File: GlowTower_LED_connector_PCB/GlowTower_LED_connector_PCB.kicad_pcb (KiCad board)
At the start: 2 copper layers, 38 x 38 mm, 12 parts, among them SW1 TS-1102S-C-A-B, U1 LED strip, U2 LED strip, U3 LED strip, U4 LED strip

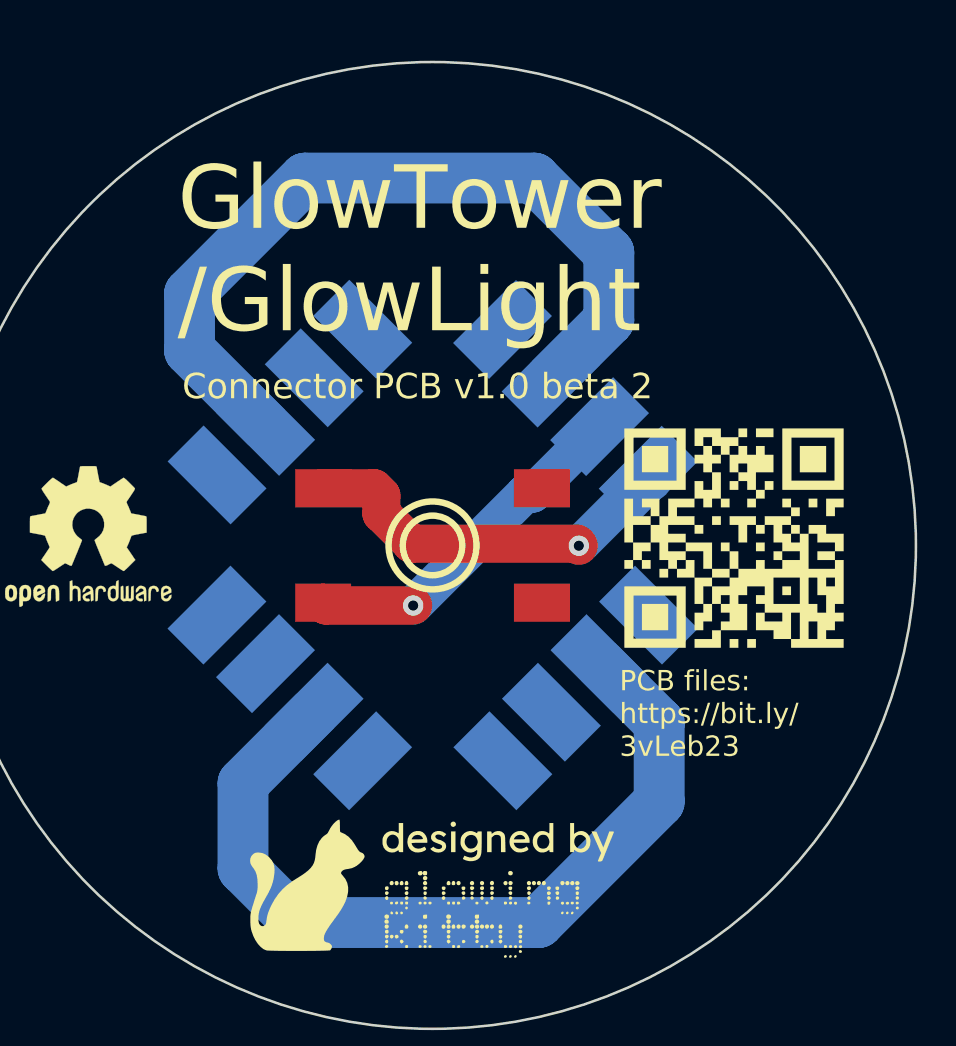
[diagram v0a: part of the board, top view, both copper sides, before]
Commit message: replaced mic and levelshifter
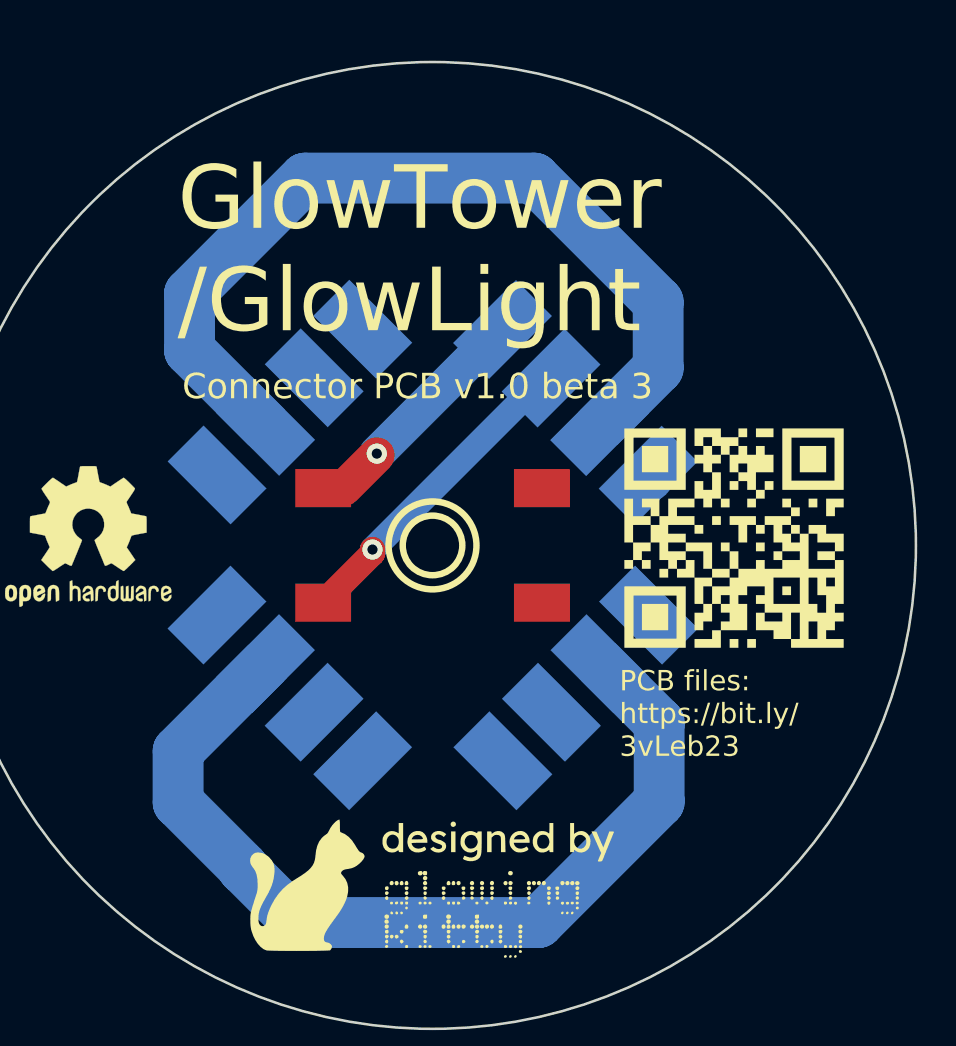
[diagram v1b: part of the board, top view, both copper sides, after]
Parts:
- moved leddirectionarrow3 2.69 mm to (92.1, 79.7)
- moved leddirectionarrow4 2.60 mm to (111.0, 64.5)
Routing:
- net BUTTON: track 15.3 -> 9.67 mm
- net Net-(U4-Pad2): track 32.9 -> 36.1 mm
- net Net-(U3-Pad2): track 31.9 -> 34.6 mm
- net GND: track 13.8 -> 12.7 mm
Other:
- board text added: "Connector PCB v1.0 beta 3"
- board text removed: "Connector PCB v1.0 beta 2"
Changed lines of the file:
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@@
     )
     (fp_rect (start -5 12.1412) (end 5 2.159) (layer "B.Fab") (width 0.12) (fill none))
-    (pad "1" smd rect (at -4.0338 0.3556 135) (size 2 3.5) (layers "B.Cu" "B.Mask")
+    (pad "1" smd rect (at 4.064 0.3556 135) (size 2 3.5) (layers "B.Cu" "B.Mask")
       (net 5 "unconnected-(U2-Pad1)") (pinfunction "5V") (pintype "bidirectional"))
-    (pad "2" smd rect (at -1.334534 0.3556 135) (size 2 3.5) (layers "B.Cu" "B.Mask")
+    (pad "2" smd rect (at 1.364732 0.3556 135) (size 2 3.5) (layers "B.Cu" "B.Mask")
       (net 15 "Net-(U4-Pad2)") (pinfunction "Data") (pintype "bidirectional"))
-    (pad "3" smd rect (at 1.364732 0.3556 135) (size 2 3.5) (layers "B.Cu" "B.Mask")
+    (pad "3" smd rect (at -1.334534 0.3556 135) (size 2 3.5) (layers "B.Cu" "B.Mask")
       (net 16 "unconnected-(U2-Pad3)") (pinfunction "GND") (pintype "bidirectional"))
-    (pad "4" smd rect (at 4.064 0.3556 135) (size 2 3.5) (layers "B.Cu" "B.Mask")
+    (pad "4" smd rect (at -4.0338 0.3556 135) (size 2 3.5) (layers "B.Cu" "B.Mask")
       (net 6 "unconnected-(U2-Pad4)") (pinfunction "BUTTON") (pintype "bidirectional"))
   )
   (footprint "LOGO" (layer "B.Cu")
-    (at 109.31 62.53 -45)
+    (at 111 64.51 -45)
     (attr board_only exclude_from_pos_files exclude_from_bom)
     (fp_text reference "leddirectionarrow4" (at 0 0 135) (layer "B.SilkS") hide
@@
     )
     (fp_rect (start -5 12.1412) (end 5 2.159) (layer "B.Fab") (width 0.12) (fill none))
-    (pad "1" smd rect (at -4.0338 0.3556 315) (size 2 3.5) (layers "B.Cu" "B.Mask")
+    (pad "1" smd rect (at 4.064 0.3556 315) (size 2 3.5) (layers "B.Cu" "B.Mask")
       (net 13 "unconnected-(U1-Pad1)") (pinfunction "5V") (pintype "bidirectional"))
-    (pad "2" smd rect (at -1.334534 0.3556 315) (size 2 3.5) (layers "B.Cu" "B.Mask")
+    (pad "2" smd rect (at 1.364732 0.3556 315) (size 2 3.5) (layers "B.Cu" "B.Mask")
       (net 14 "Net-(U3-Pad2)") (pinfunction "Data") (pintype "bidirectional"))
-    (pad "3" smd rect (at 1.364732 0.3556 315) (size 2 3.5) (layers "B.Cu" "B.Mask")
+    (pad "3" smd rect (at -1.334534 0.3556 315) (size 2 3.5) (layers "B.Cu" "B.Mask")
       (net 3 "GND") (pinfunction "GND") (pintype "bidirectional"))
-    (pad "4" smd rect (at 4.064 0.3556 315) (size 2 3.5) (layers "B.Cu" "B.Mask")
+    (pad "4" smd rect (at -4.0338 0.3556 315) (size 2 3.5) (layers "B.Cu" "B.Mask")
       (net 1 "BUTTON") (pinfunction "BUTTON") (pintype "bidirectional"))
   )
@@
   )
   (footprint "LOGO" (layer "B.Cu")
-    (at 94.08 81.55 135)
+    (at 92.1 79.73 135)
     (attr board_only exclude_from_pos_files exclude_from_bom)
     (fp_text reference "leddirectionarrow3" (at 0 0 135) (layer "B.SilkS") hide
@@
   (gr_line (start 93.760376 72.95256) (end 94.531122 72.181814) (layer "B.SilkS") (width 0.1))
   (gr_line (start 94.531122 72.181814) (end 101.60219 79.252882) (layer "B.SilkS") (width 0.1))
-  (gr_line (start 96.01 81.13) (end 94.59 79.67) (layer "B.SilkS") (width 0.15))
+  (gr_line (start 94.03 79.31) (end 92.61 77.85) (layer "B.SilkS") (width 0.15))
   (gr_line (start 101.60219 79.252882) (end 100.831444 80.023628) (layer "B.SilkS") (width 0.1))
   (gr_line (start 102.372936 80.023628) (end 101.60219 79.252882) (layer "B.SilkS") (width 0.1))
@@
   (gr_line (start 94.531122 72.181814) (end 93.760376 71.411068) (layer "B.SilkS") (width 0.1))
   (gr_line (start 108.673258 72.181814) (end 101.60219 65.110746) (layer "B.SilkS") (width 0.1))
-  (gr_line (start 112.581458 68.418117) (end 111.161458 66.958117) (layer "B.SilkS") (width 0.15))
+  (gr_line (start 106.77 62.74) (end 105.35 61.28) (layer "B.SilkS") (width 0.15))
   (gr_line (start 110.581458 66.498117) (end 109.161458 65.038117) (layer "B.SilkS") (width 0.15))
   (gr_line (start 110.67 77.8) (end 109.21 79.22) (layer "B.SilkS") (width 0.15))
@@
     (effects (font (size 2.5 2.5) (thickness 0.4)) (justify left))
   )
-  (gr_text "Connector PCB v1.0 beta 2" (at 91.76 65.94) (layer "F.SilkS")
+  (gr_text "Connector PCB v1.0 beta 3" (at 91.76 65.94) (layer "F.SilkS")
     (effects (font (size 1 1) (thickness 0.15)) (justify left))
   )
-  (segment (start 100.78 72.12) (end 99.59 70.93) (width 1.5) (layer "F.Cu") (net 1))
-  (segment (start 99.59 70.93) (end 99.59 70.23) (width 1.5) (layer "F.Cu") (net 1))
-  (segment (start 99.59 70.23) (end 99.297797 69.937797) (width 1.5) (layer "F.Cu") (net 1))
-  (segment (start 107.27 72.12) (end 100.78 72.12) (width 1.5) (layer "F.Cu") (net 1))
-  (segment (start 99.297797 69.937797) (end 97.3 69.937797) (width 1.5) (layer "F.Cu") (net 1))
-  (segment (start 107.35 72.2) (end 107.27 72.12) (width 1.5) (layer "F.Cu") (net 1))
-  (via (at 107.35 72.2) (size 0.8) (drill 0.4) (layers "F.Cu" "B.Cu") (net 1))
-  (segment (start 110.07601 69.47399) (end 107.35 72.2) (width 1.5) (layer "B.Cu") (net 1))
-  (segment (start 110.07601 69.426009) (end 110.07601 69.47399) (width 2) (layer "B.Cu") (net 1))
-  (segment (start 100.84 74.55) (end 97.412076 74.55) (width 1.5) (layer "F.Cu") (net 3))
-  (segment (start 97.412076 74.55) (end 97.3 74.437924) (width 1.5) (layer "F.Cu") (net 3))
-  (via (at 100.84 74.55) (size 0.8) (drill 0.4) (layers "F.Cu" "B.Cu") (net 3))
-  (segment (start 108.167339 67.517338) (end 105.534677 70.15) (width 1.5) (layer "B.Cu") (net 3))
-  (segment (start 105.24 70.15) (end 100.84 74.55) (width 1.5) (layer "B.Cu") (net 3))
-  (segment (start 105.534677 70.15) (end 105.45 70.15) (width 1.5) (layer "B.Cu") (net 3))
-  (segment (start 105.45 70.15) (end 105.24 70.15) (width 1.5) (layer "B.Cu") (net 3))
-  (segment (start 108.53 60.68) (end 105.6 57.75) (width 2) (layer "B.Cu") (net 14))
-  (segment (start 106.25867 65.608669) (end 108.53 63.337339) (width 2) (layer "B.Cu") (net 14))
-  (segment (start 92.05 64.517338) (end 95.041331 67.508669) (width 2) (layer "B.Cu") (net 14))
-  (segment (start 108.53 63.337339) (end 108.53 60.68) (width 2) (layer "B.Cu") (net 14))
-  (segment (start 105.6 57.75) (end 96.59 57.75) (width 2) (layer "B.Cu") (net 14))
-  (segment (start 96.59 57.75) (end 92.05 62.29) (width 2) (layer "B.Cu") (net 14))
-  (segment (start 92.05 62.29) (end 92.05 64.517338) (width 2) (layer "B.Cu") (net 14))
-  (segment (start 96.945105 78.742211) (end 94.15 81.537316) (width 2) (layer "B.Cu") (net 15))
+  (segment (start 98.112203 69.937797) (end 97.3 69.937797) (width 1) (layer "F.Cu") (net 1))
+  (segment (start 99.41 68.64) (end 98.112203 69.937797) (width 1.4) (layer "F.Cu") (net 1))
+  (segment (start 99.41 68.58) (end 99.41 68.64) (width 1) (layer "F.Cu") (net 1))
+  (via (at 99.41 68.58) (size 0.8) (drill 0.4) (layers "F.Cu" "B.Cu") (net 1))
+  (segment (start 104.35 63.7) (end 104.29 63.7) (width 1) (layer "B.Cu") (net 1))
+  (segment (start 104.29 63.7) (end 99.41 68.58) (width 1.4) (layer "B.Cu") (net 1))
+  (segment (start 99.24 72.497924) (end 97.3 74.437924) (width 1) (layer "F.Cu") (net 3))
+  (segment (start 99.24 72.35) (end 99.24 72.497924) (width 1) (layer "F.Cu") (net 3))
+  (via (at 99.24 72.35) (size 0.8) (drill 0.4) (layers "F.Cu" "B.Cu") (net 3))
+  (segment (start 106.25867 65.608669) (end 105.981331 65.608669) (width 1) (layer "B.Cu") (net 3))
+  (segment (start 105.981331 65.608669) (end 99.24 72.35) (width 1) (layer "B.Cu") (net 3))
+  (segment (start 110.07601 69.426009) (end 110.07601 69.47399) (width 2) (layer "B.Cu") (net 13))
+  (segment (start 96.59 57.75) (end 105.6 57.75) (width 2) (layer "B.Cu") (net 14))
+  (segment (start 110.47 65.214677) (end 108.167339 67.517338) (width 2) (layer "B.Cu") (net 14))
+  (segment (start 92.05 62.29) (end 96.59 57.75) (width 2) (layer "B.Cu") (net 14))
+  (segment (start 92.05 64.517338) (end 92.05 62.29) (width 2) (layer "B.Cu") (net 14))
+  (segment (start 110.47 62.62) (end 110.47 65.214677) (width 2) (layer "B.Cu") (net 14))
+  (segment (start 95.041331 67.508669) (end 92.05 64.517338) (width 2) (layer "B.Cu") (net 14))
+  (segment (start 105.6 57.75) (end 110.47 62.62) (width 2) (layer "B.Cu") (net 14))
+  (segment (start 94.15 84.84) (end 91.6 82.29) (width 2) (layer "B.Cu") (net 15))
+  (segment (start 94.15 84.88) (end 94.15 84.84) (width 2) (layer "B.Cu") (net 15))
   (segment (start 94.15 84.88) (end 96.28 87.01) (width 2) (layer "B.Cu") (net 15))
-  (segment (start 94.15 81.537316) (end 94.15 84.88) (width 2) (layer "B.Cu") (net 15))
+  (segment (start 91.6 82.29) (end 91.6 80.269978) (width 2) (layer "B.Cu") (net 15))
   (segment (start 105.76 87.01) (end 110.51 82.26) (width 2) (layer "B.Cu") (net 15))
   (segment (start 110.51 82.26) (end 110.51 79.162684) (width 2) (layer "B.Cu") (net 15))
   (segment (start 110.51 79.162684) (end 108.182211 76.834895) (width 2) (layer "B.Cu") (net 15))
+  (segment (start 91.6 80.269978) (end 95.036436 76.833542) (width 2) (layer "B.Cu") (net 15))
   (segment (start 96.28 87.01) (end 105.76 87.01) (width 2) (layer "B.Cu") (net 15))
   (zone (net 3) (net_name "GND") (layers F&B.Cu) (hatch edge 0.508)

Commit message: added release candidate 1 update
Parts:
- added U5: SMTSO3015CTJ, footprint:SMTSO3030CTJ, F.Cu at (118.6, 72.2)
- added U6: SMTSO3015CTJ, footprint:SMTSO3030CTJ, F.Cu at (84.6, 72.2)
- SW1: footprint TS-1102S-C-A-B:TS-1102S-C-A-B -> footprint:KEY-SMD_4P-L6.0-W6.0-P4.50-LS8.6
- U1, U2, U3, U4: footprint myparts:LED strip connector 4pad -> footprint:LED strip connector 4pad
- moved OSHW logo 17.6 mm to (95.8, 87.6)
- moved qrcode 11.2 mm to (108.3, 81.9)
- moved designedby 8.60 mm to (94.8, 80.4)
- moved leddirectionarrow4 1.09 mm to (111.8, 63.7)
- moved leddirectionarrow2 0.90 mm to (91.1, 63.7)
- moved leddirectionarrow1 0.90 mm to (111.6, 80.4)
- moved leddirectionarrow3 0.78 mm to (91.5, 80.3)
- moved U1 0.57 mm to (107.9, 65.9)
- moved U2 0.57 mm to (95.3, 78.5)
- moved U3 0.57 mm to (95.3, 65.9)
- moved U4 0.57 mm to (107.9, 78.4)
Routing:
- net Net-(U1-Pad2): track 34.6 -> 35.8 mm
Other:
- board size 38 x 38 mm -> 44 x 44 mm
- board text added: "Connector PCB v1.0 RC1"
- board text removed: "Connector PCB v1.0 beta 3"
